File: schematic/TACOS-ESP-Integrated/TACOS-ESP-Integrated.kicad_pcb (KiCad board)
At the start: 2 copper layers, 12 parts, among them J2 MRC522, J3 Relay, SW1 SW_ARM, U1 WeMos_D1_mini

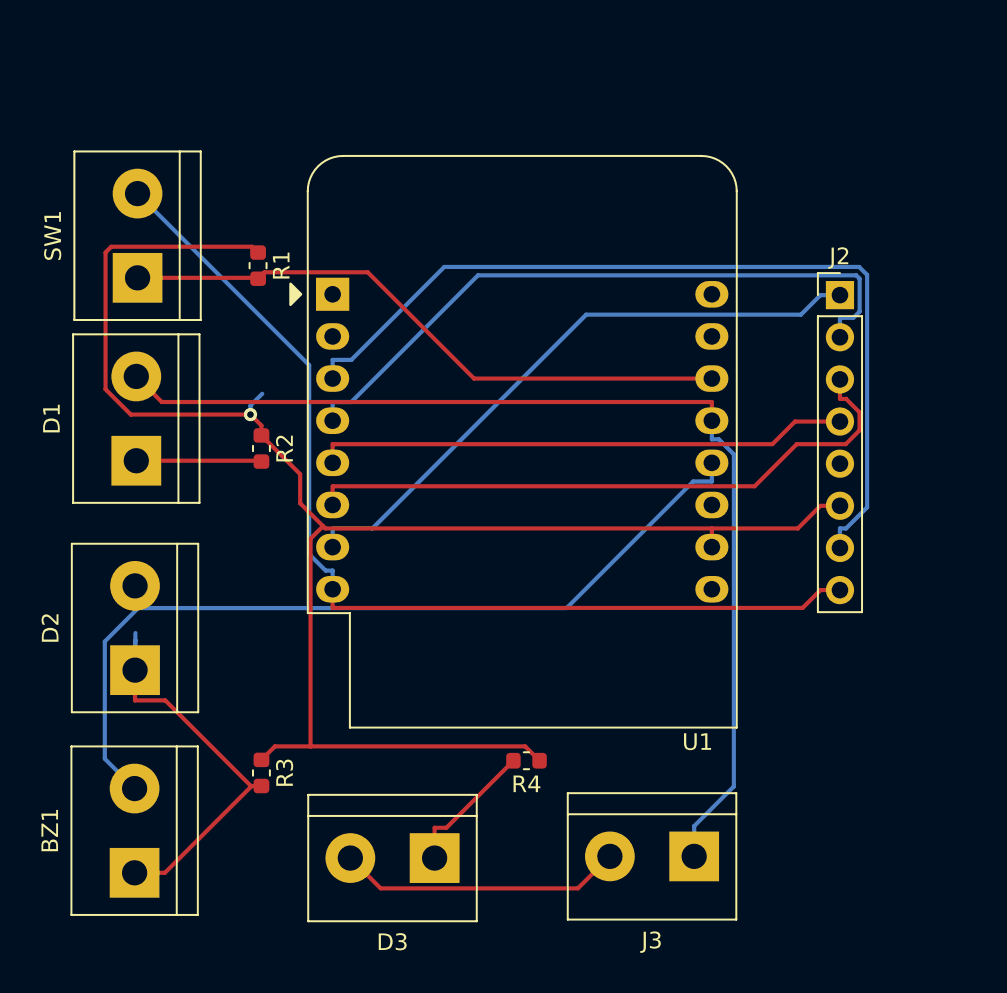
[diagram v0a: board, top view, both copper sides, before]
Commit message: Schematic updates
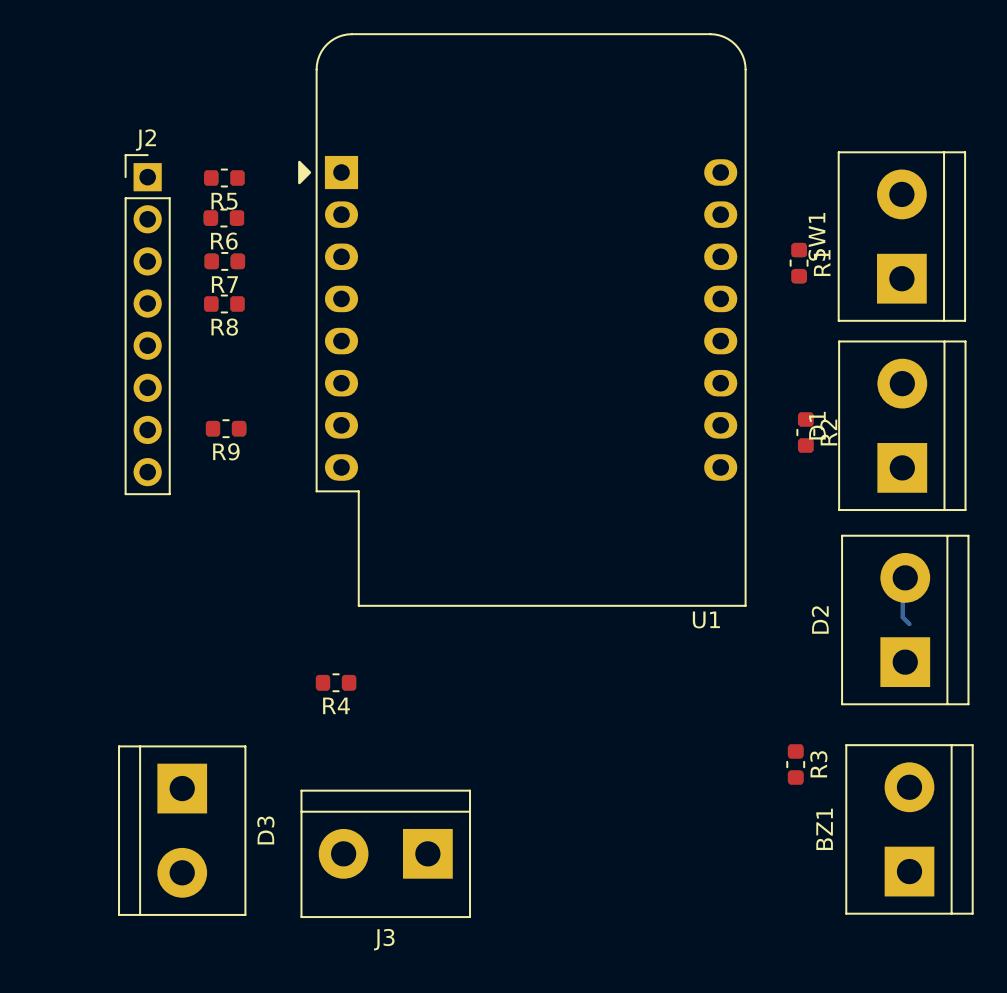
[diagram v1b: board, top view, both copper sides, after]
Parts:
- added R5: R100, Resistor_SMD:R_0603_1608Metric, F.Cu at (31.7, 47.4)
- added R6: R100, Resistor_SMD:R_0603_1608Metric, F.Cu at (31.7, 49.8)
- added R7: R100, Resistor_SMD:R_0603_1608Metric, F.Cu at (31.8, 52.5)
- added R8: R100, Resistor_SMD:R_0603_1608Metric, F.Cu at (31.7, 55.0)
- added R9: R100, Resistor_SMD:R_0603_1608Metric, F.Cu at (31.8, 62.5)
- moved BZ1 46.7 mm to (73.0, 89.2)
- moved D2 46.4 mm to (72.8, 76.6)
- moved D1 46.2 mm to (72.6, 64.9)
- moved SW1 46.1 mm to (72.6, 53.5)
- moved J2 42.3 mm to (27.1, 47.4)
- moved R2 32.8 mm to (66.8, 62.8)
- moved R1 32.6 mm to (66.4, 52.6)
- moved R3 32.2 mm to (66.2, 82.8)
- moved J3 16.1 mm to (44.0, 88.2)
- moved D3 15.8 mm to (29.2, 84.2), turned to 270 degrees
- moved R4 12.4 mm to (38.5, 77.9)
- moved U1 7.36 mm to (38.8, 47.1)
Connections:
- BZ1 pad 1: Net-(BZ1-Pad1) -> GND
- D1 pad 2: POWER_NET -> STATUS_NET
- D2 pad 1: Net-(BZ1-Pad1) -> Net-(D2-Pad1)
- D3 pad 2: Net-(D3-Pad2) -> POWER_NET
- J2 pad 1: SS -> Net-(J2-Pad1)
- J2 pad 2: SCK -> Net-(J2-Pad2)
- J2 pad 3: MOSI -> Net-(J2-Pad3)
- J2 pad 4: MISO -> Net-(J2-Pad4)
- J2 pad 7: RST -> Net-(J2-Pad7)
- J3 pad 2: Net-(D3-Pad2) -> GND
- R3 pad 2: Net-(BZ1-Pad1) -> Net-(D2-Pad1)
- U1 pad 11: (no net) -> STATUS_NET
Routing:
- net GND: track 101.1 -> 0.00 mm, vias 1 -> 0
- net POWER_NET: track 64.5 -> 0.00 mm
- net 3V3: track 61.1 -> 0.00 mm
- net RST: track 53.2 -> 0.00 mm
- net ERROR_NET: track 52.8 -> 1.51 mm
- net SCK: track 40.6 -> 0.00 mm
- net MOSI: track 38.1 -> 0.00 mm
- net SS: track 37.5 -> 0.00 mm
- net SWITCH: track 37.5 -> 0.00 mm
- net MISO: track 32.3 -> 0.00 mm
- net Net-(BZ1-Pad1): track 23.5 -> 0.00 mm
- net Net-(D3-Pad2): track 17.2 -> 0.00 mm
- net Net-(D3-Pad1): track 8.25 -> 0.00 mm
- net Net-(D1-Pad1): track 7.56 -> 0.07 mm
